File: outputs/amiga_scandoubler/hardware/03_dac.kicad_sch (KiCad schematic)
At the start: 13 parts, among them U3 ADV7125KSTZ140

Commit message: Issue 6: route the DAC bus fan-out (R/G/B, BLANK) U2 -> U3
- Reconnect the power pins at U2's top corners so the fan can pass (d6_corner_*).
- Route all 24 DAC data lines plus BLANK on F.Cu with no crossings. Only R0 uses vias (2).
- Route DAC_CLK U3 -> R24 -> U6.
- Move R10, R14, R24, R44, C29, C35, C36, C40 and C44.
- Change C42 (COMP) to 0402 so it fits clear of U3's courtyard. The schematic, netlist and manifest are updated to match.
- DRC errors 0. Unconnected items 73 -> 44 (all DAC nets complete). 54 connectivity pairs checked. The power audit is unchanged.

Co-Authored-By: Claude Opus 5.5 <noreply@anthropic.com>
Claude-Session: https://claude.ai/code/session_019f929sAJ7LRnJRRFvA6g9F
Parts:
- C42: footprint Capacitor_SMD:C_0603_1608Metric -> Capacitor_SMD:C_0402_1005Metric
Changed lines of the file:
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@@
 (property "Reference" "C42" (id 0) (at 80 103 0) (effects (font (size 1.0 1.0)) ))
 (property "Value" "100nF" (id 1) (at 80 105.8 0) (effects (font (size 1.0 1.0)) ))
-(property "Footprint" "Capacitor_SMD:C_0603_1608Metric" (id 2) (at 80 105.8 0) (effects (font (size 1.0 1.0)) hide))
+(property "Footprint" "Capacitor_SMD:C_0402_1005Metric" (id 2) (at 80 105.8 0) (effects (font (size 1.0 1.0)) hide))
 (property "Datasheet" "" (id 3) (at 80 105.8 0) (effects (font (size 1.0 1.0)) hide))
 (property "MPN" "100nF" (id 4) (at 80 105.8 0) (effects (font (size 1.0 1.0)) hide))

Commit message: Select LCSC parts with live JLCPCB stock/price (135 of 139 parts)
- r11_select.py queries JLCPCB's public component search. It matches package and spec (C/V/dielectric, R/tolerance, 0.1% thin film) and ranks basic > preferred > stock.
- Results are in fab/v030wip/parts_selection.csv/.json. r11_apply.py writes LCSC/MPN into the manifest, schematic symbols and netlist.
- Open items:
  - U1 TVP7002: stock 4.
  - J1/J2 CONEC 33DSMT1-E15SNCT: stock 0.
  - Y1 ECS-3225MVLC-270: stock 4. YXC OT2EL4C4JI-111OLP-27M (C5203549) is a datasheet-checked drop-in candidate.
- Nets unchanged (595 nodes match the board). The audit passes. Nothing ordered.

Co-Authored-By: Claude Opus 5.5 <noreply@anthropic.com>
Claude-Session: https://claude.ai/code/session_019f929sAJ7LRnJRRFvA6g9F
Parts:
- C42: LCSC (none) -> C1525; MPN 100nF -> CL05B104KO5NNNC
- C43, C44, C45, C46: LCSC (none) -> C14663; MPN 100nF -> CC0603KRX7R9BB104
- C47: LCSC (none) -> C15850; MPN 10uF -> CL21A106KAYNNNE
- R10: LCSC (none) -> C861466; MPN 536R 0.1% -> RT0603BRD07536RL
- R11, R12, R13: LCSC (none) -> C319466; MPN 75R 0.1% -> AR03BTCX0750
- R14: LCSC (none) -> C25804; MPN 10k -> 0603WAF1002T5E
- R44: LCSC (none) -> C23162; MPN 4.7k -> 0603WAF4701T5E
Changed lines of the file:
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@@
 (property "Footprint" "Capacitor_SMD:C_0402_1005Metric" (id 2) (at 80 105.8 0) (effects (font (size 1.0 1.0)) hide))
 (property "Datasheet" "" (id 3) (at 80 105.8 0) (effects (font (size 1.0 1.0)) hide))
-(property "MPN" "100nF" (id 4) (at 80 105.8 0) (effects (font (size 1.0 1.0)) hide))
-(property "LCSC" "" (id 5) (at 80 105.8 0) (effects (font (size 1.0 1.0)) hide))
+(property "MPN" "CL05B104KO5NNNC" (id 4) (at 80 105.8 0) (effects (font (size 1.0 1.0)) hide))
+(property "LCSC" "C1525" (id 5) (at 80 105.8 0) (effects (font (size 1.0 1.0)) hide))
 (pin "1")
 (pin "2")
@@
 (property "Footprint" "Capacitor_SMD:C_0603_1608Metric" (id 2) (at 200 105.8 0) (effects (font (size 1.0 1.0)) hide))
 (property "Datasheet" "" (id 3) (at 200 105.8 0) (effects (font (size 1.0 1.0)) hide))
-(property "MPN" "100nF" (id 4) (at 200 105.8 0) (effects (font (size 1.0 1.0)) hide))
-(property "LCSC" "" (id 5) (at 200 105.8 0) (effects (font (size 1.0 1.0)) hide))
+(property "MPN" "CC0603KRX7R9BB104" (id 4) (at 200 105.8 0) (effects (font (size 1.0 1.0)) hide))
+(property "LCSC" "C14663" (id 5) (at 200 105.8 0) (effects (font (size 1.0 1.0)) hide))
 (pin "1")
 (pin "2")
@@
 (property "Footprint" "Resistor_SMD:R_0603_1608Metric" (id 2) (at 320 105.8 0) (effects (font (size 1.0 1.0)) hide))
 (property "Datasheet" "" (id 3) (at 320 105.8 0) (effects (font (size 1.0 1.0)) hide))
-(property "MPN" "536R 0.1%" (id 4) (at 320 105.8 0) (effects (font (size 1.0 1.0)) hide))
-(property "LCSC" "" (id 5) (at 320 105.8 0) (effects (font (size 1.0 1.0)) hide))
+(property "MPN" "RT0603BRD07536RL" (id 4) (at 320 105.8 0) (effects (font (size 1.0 1.0)) hide))
+(property "LCSC" "C861466" (id 5) (at 320 105.8 0) (effects (font (size 1.0 1.0)) hide))
 (pin "1")
 (pin "2")
@@
 (property "Footprint" "Resistor_SMD:R_0603_1608Metric" (id 2) (at 80 135.8 0) (effects (font (size 1.0 1.0)) hide))
 (property "Datasheet" "" (id 3) (at 80 135.8 0) (effects (font (size 1.0 1.0)) hide))
-(property "MPN" "75R 0.1%" (id 4) (at 80 135.8 0) (effects (font (size 1.0 1.0)) hide))
-(property "LCSC" "" (id 5) (at 80 135.8 0) (effects (font (size 1.0 1.0)) hide))
+(property "MPN" "AR03BTCX0750" (id 4) (at 80 135.8 0) (effects (font (size 1.0 1.0)) hide))
+(property "LCSC" "C319466" (id 5) (at 80 135.8 0) (effects (font (size 1.0 1.0)) hide))
 (pin "1")
 (pin "2")
@@
 (property "Footprint" "Resistor_SMD:R_0603_1608Metric" (id 2) (at 200 135.8 0) (effects (font (size 1.0 1.0)) hide))
 (property "Datasheet" "" (id 3) (at 200 135.8 0) (effects (font (size 1.0 1.0)) hide))
-(property "MPN" "75R 0.1%" (id 4) (at 200 135.8 0) (effects (font (size 1.0 1.0)) hide))
-(property "LCSC" "" (id 5) (at 200 135.8 0) (effects (font (size 1.0 1.0)) hide))
+(property "MPN" "AR03BTCX0750" (id 4) (at 200 135.8 0) (effects (font (size 1.0 1.0)) hide))
+(property "LCSC" "C319466" (id 5) (at 200 135.8 0) (effects (font (size 1.0 1.0)) hide))
 (pin "1")
 (pin "2")
@@
 (property "Footprint" "Resistor_SMD:R_0603_1608Metric" (id 2) (at 320 135.8 0) (effects (font (size 1.0 1.0)) hide))
 (property "Datasheet" "" (id 3) (at 320 135.8 0) (effects (font (size 1.0 1.0)) hide))
-(property "MPN" "75R 0.1%" (id 4) (at 320 135.8 0) (effects (font (size 1.0 1.0)) hide))
-(property "LCSC" "" (id 5) (at 320 135.8 0) (effects (font (size 1.0 1.0)) hide))
+(property "MPN" "AR03BTCX0750" (id 4) (at 320 135.8 0) (effects (font (size 1.0 1.0)) hide))
+(property "LCSC" "C319466" (id 5) (at 320 135.8 0) (effects (font (size 1.0 1.0)) hide))
 (pin "1")
 (pin "2")
@@
 (property "Footprint" "Capacitor_SMD:C_0603_1608Metric" (id 2) (at 80 162.8 0) (effects (font (size 1.0 1.0)) hide))
 (property "Datasheet" "" (id 3) (at 80 162.8 0) (effects (font (size 1.0 1.0)) hide))
-(property "MPN" "100nF" (id 4) (at 80 162.8 0) (effects (font (size 1.0 1.0)) hide))
-(property "LCSC" "" (id 5) (at 80 162.8 0) (effects (font (size 1.0 1.0)) hide))
+(property "MPN" "CC0603KRX7R9BB104" (id 4) (at 80 162.8 0) (effects (font (size 1.0 1.0)) hide))
+(property "LCSC" "C14663" (id 5) (at 80 162.8 0) (effects (font (size 1.0 1.0)) hide))
 (pin "1")
 (pin "2")
@@
 (property "Footprint" "Capacitor_SMD:C_0603_1608Metric" (id 2) (at 200 162.8 0) (effects (font (size 1.0 1.0)) hide))
 (property "Datasheet" "" (id 3) (at 200 162.8 0) (effects (font (size 1.0 1.0)) hide))
-(property "MPN" "100nF" (id 4) (at 200 162.8 0) (effects (font (size 1.0 1.0)) hide))
-(property "LCSC" "" (id 5) (at 200 162.8 0) (effects (font (size 1.0 1.0)) hide))
+(property "MPN" "CC0603KRX7R9BB104" (id 4) (at 200 162.8 0) (effects (font (size 1.0 1.0)) hide))
+(property "LCSC" "C14663" (id 5) (at 200 162.8 0) (effects (font (size 1.0 1.0)) hide))
 (pin "1")
 (pin "2")
@@
 (property "Footprint" "Capacitor_SMD:C_0603_1608Metric" (id 2) (at 320 162.8 0) (effects (font (size 1.0 1.0)) hide))
 (property "Datasheet" "" (id 3) (at 320 162.8 0) (effects (font (size 1.0 1.0)) hide))
-(property "MPN" "100nF" (id 4) (at 320 162.8 0) (effects (font (size 1.0 1.0)) hide))
-(property "LCSC" "" (id 5) (at 320 162.8 0) (effects (font (size 1.0 1.0)) hide))
+(property "MPN" "CC0603KRX7R9BB104" (id 4) (at 320 162.8 0) (effects (font (size 1.0 1.0)) hide))
+(property "LCSC" "C14663" (id 5) (at 320 162.8 0) (effects (font (size 1.0 1.0)) hide))
 (pin "1")
 (pin "2")
@@
 (property "Footprint" "Capacitor_SMD:C_0805_2012Metric" (id 2) (at 80 185.8 0) (effects (font (size 1.0 1.0)) hide))
 (property "Datasheet" "" (id 3) (at 80 185.8 0) (effects (font (size 1.0 1.0)) hide))
-(property "MPN" "10uF" (id 4) (at 80 185.8 0) (effects (font (size 1.0 1.0)) hide))
-(property "LCSC" "" (id 5) (at 80 185.8 0) (effects (font (size 1.0 1.0)) hide))
+(property "MPN" "CL21A106KAYNNNE" (id 4) (at 80 185.8 0) (effects (font (size 1.0 1.0)) hide))
+(property "LCSC" "C15850" (id 5) (at 80 185.8 0) (effects (font (size 1.0 1.0)) hide))
 (pin "1")
 (pin "2")
@@
 (property "Footprint" "Resistor_SMD:R_0603_1608Metric" (id 2) (at 200 185.8 0) (effects (font (size 1.0 1.0)) hide))
 (property "Datasheet" "" (id 3) (at 200 185.8 0) (effects (font (size 1.0 1.0)) hide))
-(property "MPN" "10k" (id 4) (at 200 185.8 0) (effects (font (size 1.0 1.0)) hide))
-(property "LCSC" "" (id 5) (at 200 185.8 0) (effects (font (size 1.0 1.0)) hide))
+(property "MPN" "0603WAF1002T5E" (id 4) (at 200 185.8 0) (effects (font (size 1.0 1.0)) hide))
+(property "LCSC" "C25804" (id 5) (at 200 185.8 0) (effects (font (size 1.0 1.0)) hide))
 (pin "1")
 (pin "2")
@@
 (property "Footprint" "Resistor_SMD:R_0603_1608Metric" (id 2) (at 290 185.8 0) (effects (font (size 1.0 1.0)) hide))
 (property "Datasheet" "" (id 3) (at 290 185.8 0) (effects (font (size 1.0 1.0)) hide))
-(property "MPN" "4.7k" (id 4) (at 290 185.8 0) (effects (font (size 1.0 1.0)) hide))
-(property "LCSC" "" (id 5) (at 290 185.8 0) (effects (font (size 1.0 1.0)) hide))
+(property "MPN" "0603WAF4701T5E" (id 4) (at 290 185.8 0) (effects (font (size 1.0 1.0)) hide))
+(property "LCSC" "C23162" (id 5) (at 290 185.8 0) (effects (font (size 1.0 1.0)) hide))
 (pin "1")
 (pin "2")

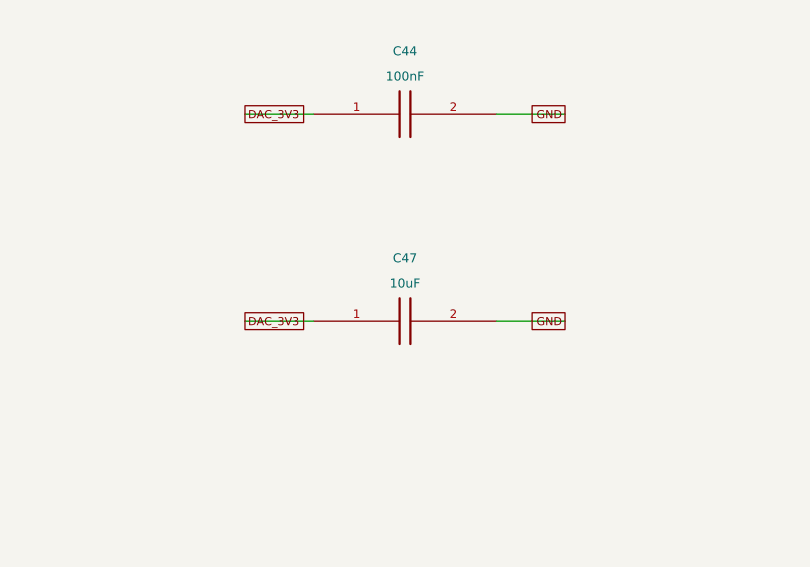
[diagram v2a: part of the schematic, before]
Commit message: JLC DFM/order fixes: move vias off pads, widen J3 slots, re-place silk, replace L1-L3, merge C15850 BOM line
- dfm_vias.py: 31 vias moved (pad gap >= 0.15 mm), via-in-pad removed on C56/C58/C59/C60/C71
- dfm_fix2.py: C71/C29 +0.4 mm, J3 footprint with 0.8 mm slots, C15850 values unified
- dfm_silk.py: 50 reference texts re-placed away from pads/holes
- L1-L3 -> Taiyo Yuden NRS4018T2R2MDGJ (C92959, EasyEDA footprint available)
- DRC 0 errors / 0 unconnected, audit PASS, ERC clean, fab outputs regenerated

Co-Authored-By: Claude Opus 5.5 <noreply@anthropic.com>
Claude-Session: https://claude.ai/code/session_019f929sAJ7LRnJRRFvA6g9F
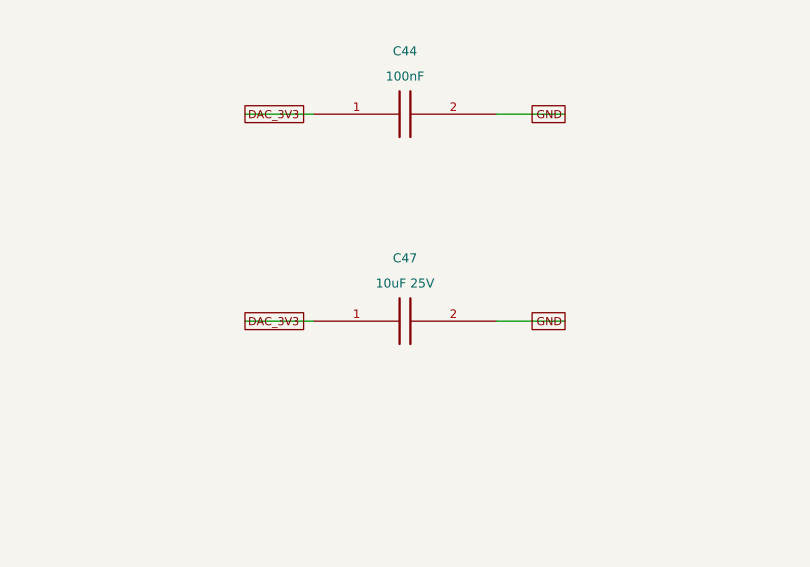
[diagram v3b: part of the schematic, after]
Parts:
- C47: value 10uF -> 10uF 25V
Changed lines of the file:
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@@
 (symbol (lib_id "Amiga:C") (at 80 190 0) (unit 1) (in_bom yes) (on_board yes)
 (property "Reference" "C47" (id 0) (at 80 183 0) (effects (font (size 1.0 1.0)) ))
-(property "Value" "10uF" (id 1) (at 80 185.8 0) (effects (font (size 1.0 1.0)) ))
+(property "Value" "10uF 25V" (id 1) (at 80 185.8 0) (effects (font (size 1.0 1.0)) ))
 (property "Footprint" "Capacitor_SMD:C_0805_2012Metric" (id 2) (at 80 185.8 0) (effects (font (size 1.0 1.0)) hide))
 (property "Datasheet" "" (id 3) (at 80 185.8 0) (effects (font (size 1.0 1.0)) hide))
@@
 (path "/d7285cc1-01a7-52b5-b1b4-a16a6a4410c1/8323dc3f-5117-52a0-997b-42f9a0685bef/a216a327-0d42-586b-96a4-cccc07280ed5" (reference "C45") (unit 1) (value "100nF") (footprint "Capacitor_SMD:C_0603_1608Metric"))
 (path "/d7285cc1-01a7-52b5-b1b4-a16a6a4410c1/8323dc3f-5117-52a0-997b-42f9a0685bef/75d6a04d-4053-5d5c-b82f-526256d4ef3d" (reference "C46") (unit 1) (value "100nF") (footprint "Capacitor_SMD:C_0603_1608Metric"))
-(path "/d7285cc1-01a7-52b5-b1b4-a16a6a4410c1/8323dc3f-5117-52a0-997b-42f9a0685bef/171abb46-6adc-542f-9caa-96a2960db62d" (reference "C47") (unit 1) (value "10uF") (footprint "Capacitor_SMD:C_0805_2012Metric"))
+(path "/d7285cc1-01a7-52b5-b1b4-a16a6a4410c1/8323dc3f-5117-52a0-997b-42f9a0685bef/171abb46-6adc-542f-9caa-96a2960db62d" (reference "C47") (unit 1) (value "10uF 25V") (footprint "Capacitor_SMD:C_0805_2012Metric"))
 (path "/d7285cc1-01a7-52b5-b1b4-a16a6a4410c1/8323dc3f-5117-52a0-997b-42f9a0685bef/5da0d2b0-c2a6-5faa-badb-69924feeb36a" (reference "R14") (unit 1) (value "10k") (footprint "Resistor_SMD:R_0603_1608Metric"))
 (path "/d7285cc1-01a7-52b5-b1b4-a16a6a4410c1/8323dc3f-5117-52a0-997b-42f9a0685bef/446f5906-3a7c-5324-9597-55e029bb97d9" (reference "R44") (unit 1) (value "4.7k") (footprint "Resistor_SMD:R_0603_1608Metric"))
